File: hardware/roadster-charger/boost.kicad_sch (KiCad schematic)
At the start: 25 parts

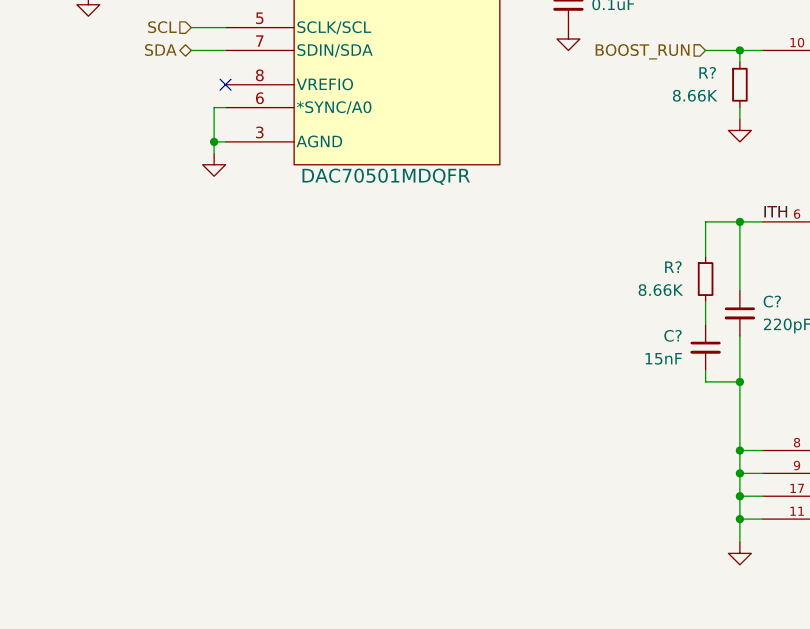
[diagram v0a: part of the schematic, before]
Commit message: add note to DAC circuit, swap DAC to model with 0V output at boot
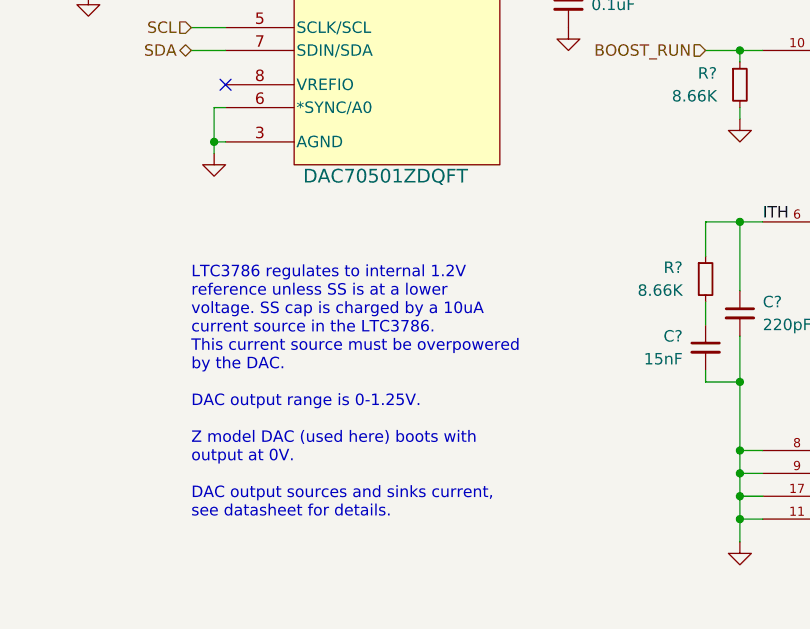
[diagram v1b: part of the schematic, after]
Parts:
- U?: value DAC70501MDQFR -> DAC70501ZDQFT; MPN DAC70501MDQFR -> DAC70501ZDQFT
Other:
- note added: "LTC3786 regulates to internal 1.2V reference unless SS is at a lower voltage. SS cap is charged by a 10uA current source in the LTC3786. This current source must be overpowered by the DAC. DAC output range is 0-1.25V. Z model DAC (used here) boots with output at 0V. DAC output sources and sinks current, see datasheet for details."
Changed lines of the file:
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@@
+    (effects (font (size 1.27 1.27)) (justify left bottom))
+  )
+  (text "LTC3786 regulates to internal 1.2V\nreference unless SS is at a lower \nvoltage. SS cap is charged by a 10uA\ncurrent source in the LTC3786.\nThis current source must be overpowered \nby the DAC. \n\nDAC output range is 0-1.25V.\n\nZ model DAC (used here) boots with\noutput at 0V.\n\nDAC output sources and sinks current,\nsee datasheet for details."
+    (at 130.81 168.91 0)
     (effects (font (size 1.27 1.27)) (justify left bottom))
   )
@@
       (effects (font (size 1.524 1.524)))
     )
-    (property "Value" "DAC70501MDQFR" (at 152.4 130.81 0)
+    (property "Value" "DAC70501ZDQFT" (at 152.4 130.81 0)
       (effects (font (size 1.524 1.524)))
     )
@@
       (effects (font (size 1.27 1.27) italic) hide)
     )
-    (property "Datasheet" "DAC70501MDQFR" (at 134.62 107.95 0)
+    (property "Datasheet" "https://www.ti.com/lit/ds/symlink/dac70501.pdf?ts=1702864708763&ref_url=https%253A%252F%252Fwww.ti.com%252Fproduct%252FDAC70501" (at 134.62 107.95 0)
       (effects (font (size 1.27 1.27) italic) hide)
     )
-    (property "MPN" "DAC70501MDQFR" (at 134.62 111.76 0)
+    (property "MPN" "DAC70501ZDQFT" (at 134.62 111.76 0)
       (effects (font (size 1.27 1.27)) hide)
     )

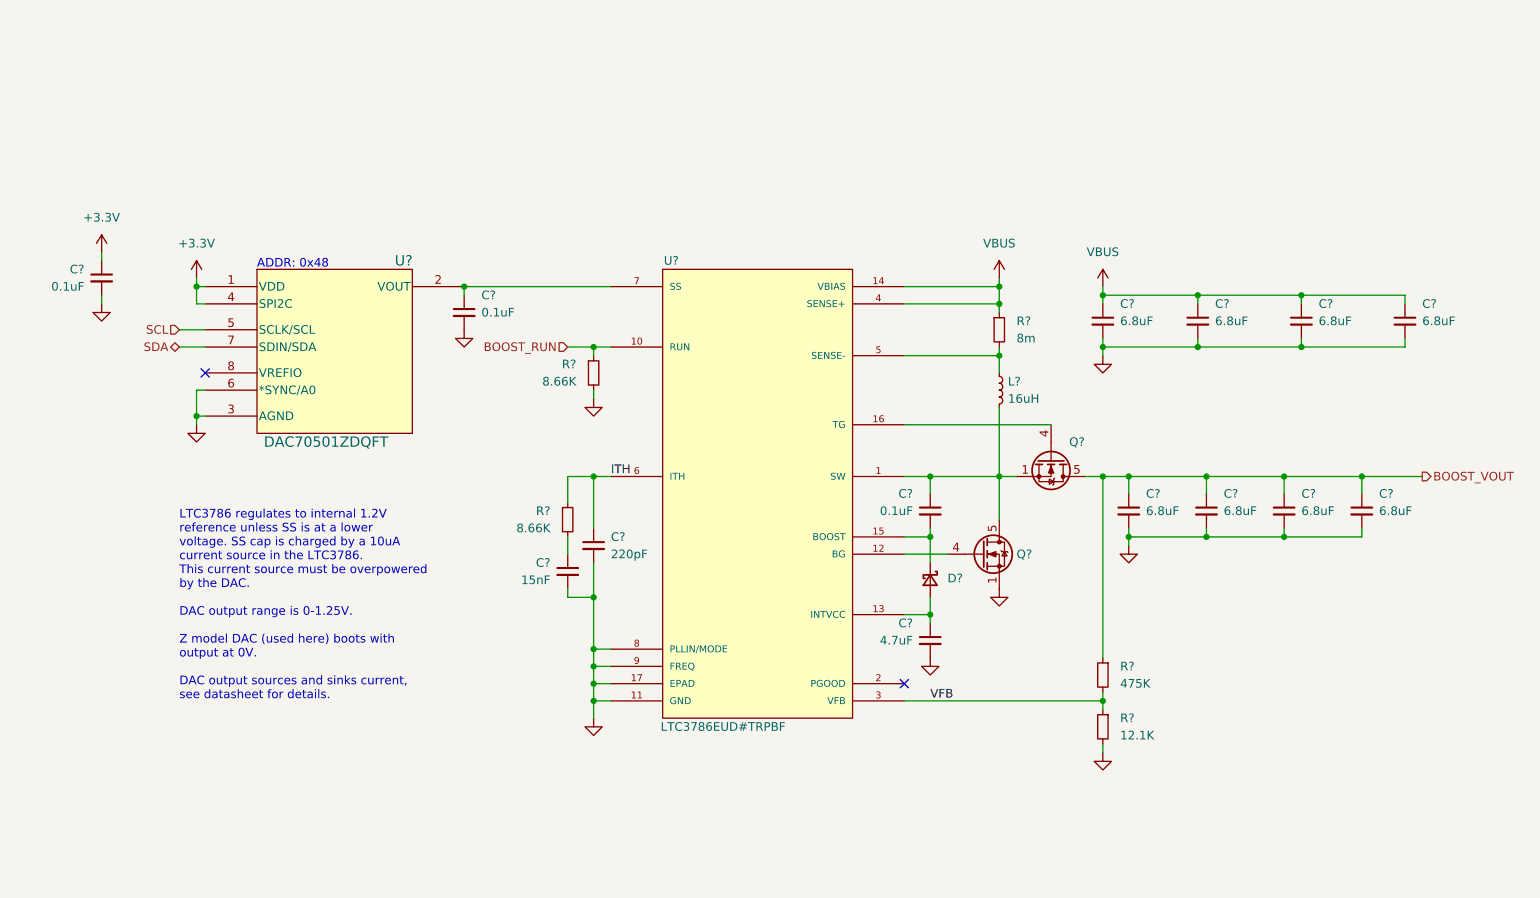
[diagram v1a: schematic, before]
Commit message: connect FUSB307 vbus pin
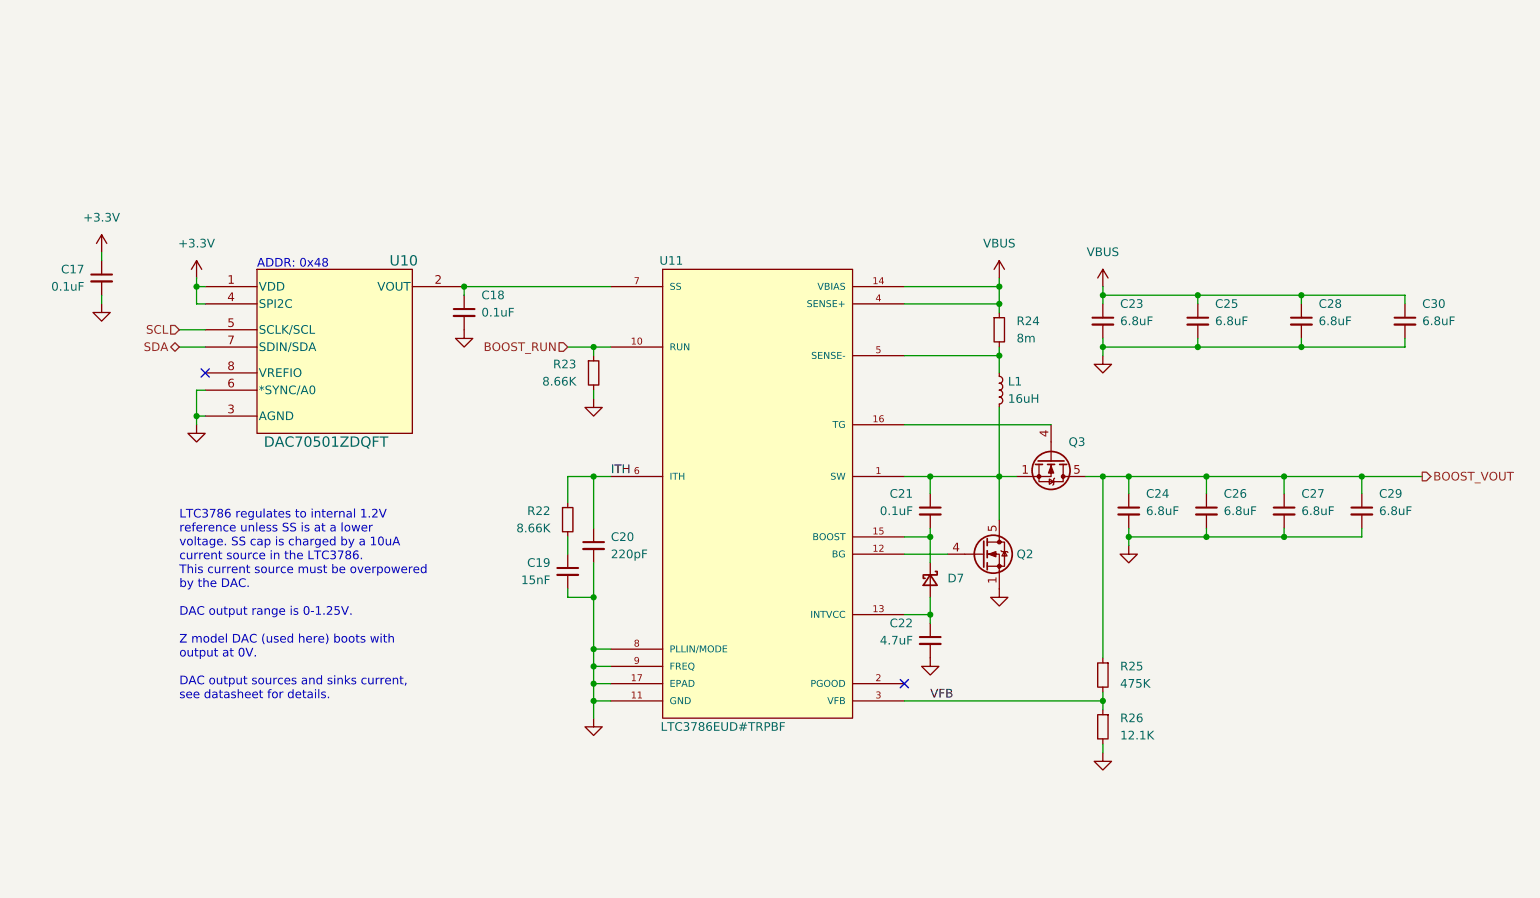
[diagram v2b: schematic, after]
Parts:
- gave numbers to parts that had none: 25

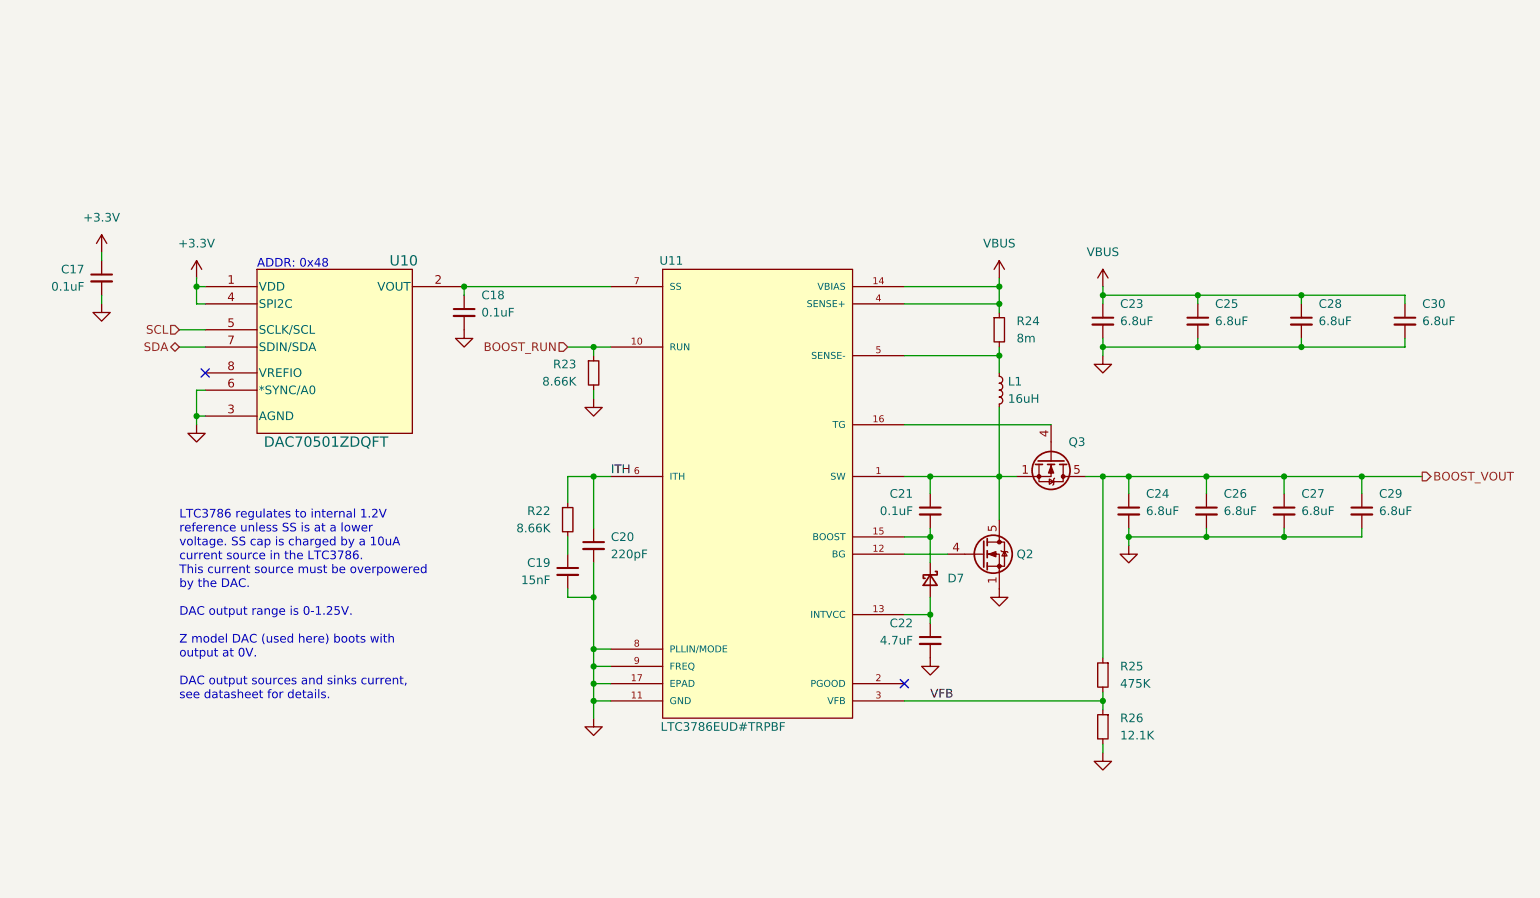
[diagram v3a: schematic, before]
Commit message: Rough rev 2 layout
Move boost run pin to GPIO6 to avoid hard coded UART output
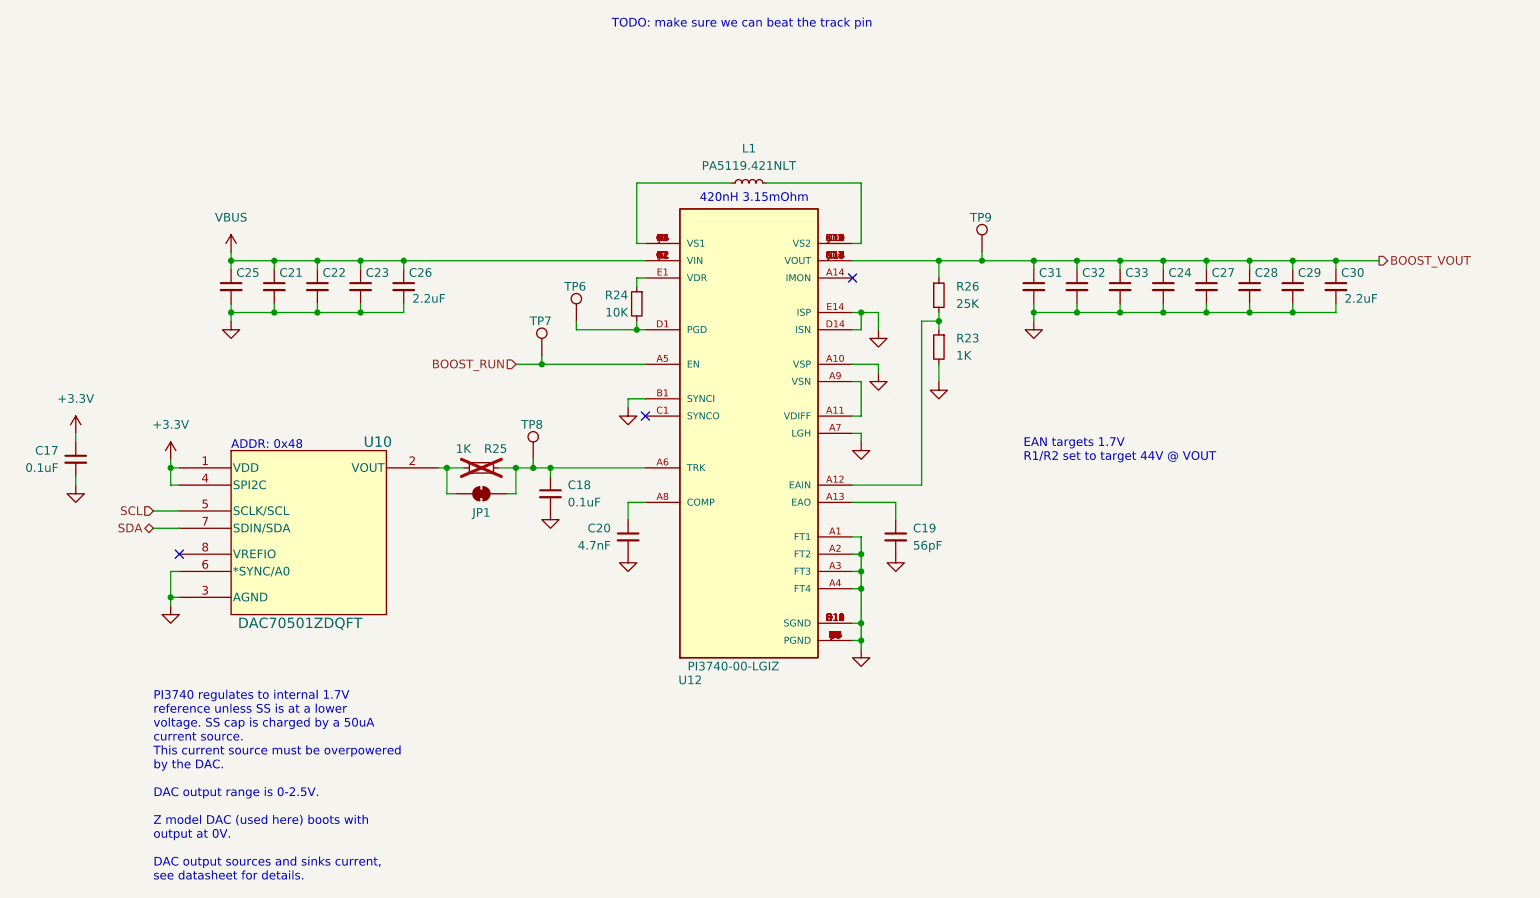
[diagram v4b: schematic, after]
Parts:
- removed D7: D_Schottky_Small, Diode_SMD:D_SOD-323, symbol Device:D_Schottky_Small
- removed Q2, Q3: CSD19532Q5B, Package_TO_SOT_SMD:TDSON-8-1, symbol Transistor_FET:CSD19532Q5B
- removed R22: 8.66K, Resistor_SMD:R_0603_1608Metric, symbol Device:R_Small
- removed U11: LTC3786EUD#TRPBF, LTC3786EUD_TRPBF:QFN-16_UD, symbol LTC3786EUD_TRPBF:LTC3786EUD#TRPBF
- added C31, C32, C33: 2.2uF, Capacitor_SMD:C_1210_3225Metric, symbol Device:C_Small
- added JP1: SolderJumper_2_Bridged, Jumper:SolderJumper-2_P1.3mm_Bridged2Bar_RoundedPad1.0x1.5mm, symbol Jumper:SolderJumper_2_Bridged
- added TP6, TP7, TP8, TP9: RCU-0C, RCU-0C:TP+195X110, symbol Connector:TestPoint
- added U12: PI3740-00-LGIZ, PI3740-00-LGIZ:LGA108S100P10X14_1000X1400X263N, symbol PI3740-00-LGIZ:PI3740-00-LGIZ
- C19: value 15nF -> 56pF; MPN C0603C153K4REC7867 -> C0603C560G5GAC7867
- C20: value 220pF -> 4.7nF; MPN C0603C221K1RAC7867 -> C0603C472K4RECAUTO7411
- C21: value 0.1uF -> 2.2uF; footprint Capacitor_SMD:C_0805_2012Metric -> Capacitor_SMD:C_1210_3225Metric; MPN CC0805KRX7R9BB104 -> GRM32ER72A225KA35
- C22: value 4.7uF -> 2.2uF; footprint Capacitor_SMD:C_0603_1608Metric -> Capacitor_SMD:C_1210_3225Metric; MPN C1608X5R1E475K080AC -> GRM32ER72A225KA35
- C23, C24, C25, C26, C27, C28, C29, C30: value 6.8uF -> 2.2uF; footprint Capacitor_SMD:C_1812_4532Metric -> Capacitor_SMD:C_1210_3225Metric; MPN C4532X7R1H685K -> GRM32ER72A225KA35
- L1: value 16uH -> PA5119.421NLT; footprint PA2050.193NL:IND_PA2050.193NL -> footprints:SMT_119.421NLT_PUL; MPN PA2050.163NL -> PA5119.421NLT
- R23: value 8.66K -> 1K; MPN RC0603FR-078K66L -> RC0603FR-071KL
- R24: value 8m -> 10K; footprint Resistor_SMD:R_1206_3216Metric -> Resistor_SMD:R_0603_1608Metric; MPN WSLP12068L000FEA -> RMCF0603FT10K0
- R25: value 475K -> 1K; MPN RC0603FR-07475KL -> DNP; now not fitted
- R26: value 12.1K -> 25K; MPN RC0603FR-1312K1L -> RT1206BRD0725KL
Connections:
- net BOOST_RUN: now also TP7.1, U12.A5 (EN); no longer R23.1
- net BOOST_VOUT: now also C28.1, C30.1, R26.1, C31.1, C32.1, C33.1, TP9.1, U12.G13 (VOUT), U12.G14 (VOUT), U12.H13 (VOUT), U12.H14 (VOUT), U12.J13 (VOUT), U12.J14 (VOUT), U12.K13 (VOUT), U12.K14 (VOUT); no longer C26.1, R25.1
- net GND: now also C21.2, C31.2, C32.2, C33.2, U12.A1 (FT1), U12.A10 (VSP), U12.A2 (FT2), U12.A3 (FT3), U12.A4 (FT4), U12.A7 (LGH), U12.B1 (SYNCI), U12.B10 (SGND), U12.B11 (SGND), U12.B12 (SGND), U12.B13 (SGND), U12.B14 (SGND), U12.B2 (PGND), U12.B3 (PGND), U12.B4 (PGND), U12.B5 (PGND), U12.B6 (PGND), U12.B7 (PGND), U12.B8 (PGND), U12.B9 (PGND), U12.C10 (SGND), U12.C11 (SGND), U12.C12 (SGND), U12.C2 (PGND), U12.C3 (PGND), U12.C4 (PGND), U12.C5 (PGND), U12.C6 (PGND), U12.C7 (PGND), U12.C8 (PGND), U12.C9 (PGND), U12.D10 (SGND), U12.D11 (SGND), U12.D12 (SGND), U12.D14 (ISN), U12.D2 (PGND), U12.D3 (PGND), U12.D4 (PGND), U12.D5 (PGND), U12.D6 (PGND), U12.D7 (PGND), U12.D8 (PGND), U12.D9 (PGND), U12.E10 (SGND), U12.E11 (SGND), U12.E12 (SGND), U12.E14 (ISP), U12.E2 (PGND), U12.E3 (PGND), U12.E4 (PGND), U12.E5 (PGND), U12.E6 (PGND), U12.E7 (PGND), U12.E8 (PGND), U12.E9 (PGND), U12.F7 (PGND), U12.F8 (PGND), U12.G7 (PGND), U12.G8 (PGND), U12.H7 (PGND), U12.H8 (PGND), U12.J7 (PGND), U12.J8 (PGND), U12.K7 (PGND), U12.K8 (PGND); no longer R26.2
- net VBUS: now also C21.1, C22.1, C26.1, U12.G1 (VIN), U12.G2 (VIN), U12.H1 (VIN), U12.H2 (VIN), U12.J1 (VIN), U12.J2 (VIN), U12.K1 (VIN), U12.K2 (VIN); no longer C28.1, C30.1, R24.1
- net at U10.2 (VOUT): now also R25.2, JP1.1 (A); no longer C18.1
- net at L1.2: now also U12.G4 (VS1), U12.G5 (VS1), U12.H4 (VS1), U12.H5 (VS1), U12.J4 (VS1), U12.J5 (VS1), U12.K4 (VS1), U12.K5 (VS1); no longer C21.1
- net at C19.1: now also U12.A13 (EAO)
- net at L1.1: now also U12.G10 (VS2), U12.G11 (VS2), U12.H10 (VS2), U12.H11 (VS2), U12.J10 (VS2), U12.J11 (VS2), U12.K10 (VS2), U12.K11 (VS2); no longer R24.2
- net ITH: no longer names the net of C20.1
- net ITH: now also U12.A8 (COMP)
- removed net VFB: R25.2, R26.1
- new net: R23.1, R26.2, U12.A12 (EAIN)
- new net: C18.1, JP1.2 (B), R25.1, TP8.1, U12.A6 (TRK)
- new net: R24.1, U12.E1 (VDR)
- new net: R24.2, TP6.1, U12.D1 (PGD)
- new net: U12.A11 (VDIFF), U12.A9 (VSN)
- no-connect marks 2 -> 3
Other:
- note added: "420nH 3.15mOhm"
- note added: "EAN targets 1.7V R1/R2 set to target 44V @ VOUT"
- note added: "PI3740 regulates to internal 1.7V reference unless SS is at a lower voltage. SS cap is charged by a 50uA current source. This current source must be overpowered by the DAC. DAC output range is 0-2.5V. Z model DAC (used here) boots with output at 0V. DAC output sources and sinks current, see datasheet for details."
- note added: "TODO: make sure we can beat the track pin"
- note removed: "LTC3786 regulates to internal 1.2V reference unless SS is at a lower voltage. SS cap is charged by a 10uA current source in the LTC3786. This current source must be overpowered by the DAC. DAC output range is 0-1.25V. Z model DAC (used here) boots with output at 0V. DAC output sources and sinks current, see datasheet for details."
- moved on the sheet: C17, C18, U10

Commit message: add debug connected LED
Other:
- note removed: "TODO: make sure we can beat the track pin"
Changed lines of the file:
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@@
-		)
-	)
-	(text "TODO: make sure we can beat the track pin"
-		(exclude_from_sim no)
-		(at 213.614 69.342 0)
-		(effects
-			(font
-				(size 1.27 1.27)
-			)
 		)
 	)
